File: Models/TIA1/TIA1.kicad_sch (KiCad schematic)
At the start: 0 parts

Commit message: Save progress
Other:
- note added: "Input: 15V power Input: -15V power Input: current Output: voltage Ground connection(s) not yet elaborated"
- note removed: "Input: 15V power (grounded interconnect) Input: -15V power (grounded interconnect) Input: current Output: voltage (grounded interconnect)"
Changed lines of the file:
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@@
 	(generator_version "9.0")
 	(paper "A4")
-	(text "Input: 15V power (grounded interconnect)\nInput: -15V power (grounded interconnect)\nInput: current\nOutput: voltage (grounded interconnect)"
+	(text "Input: 15V power\nInput: -15V power\nInput: current\nOutput: voltage\n\nGround connection(s) not yet elaborated"
 		(exclude_from_sim no)
 		(at 158.242 76.962 0)
@@
 		)
 		(instances
-			(project "TransimpedanceAmplifier"
+			(project "TIA1"
 				(path "/f19129fc-f916-4692-924c-ee308c6b3e1d"
 					(page "2")

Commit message: Save progress
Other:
- note added: "Input: 15V power Input: -15V power Input: current Output: voltage"
- note removed: "Input: 15V power Input: -15V power Input: current Output: voltage Ground connection(s) not yet elaborated"
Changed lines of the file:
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@@
 	(generator_version "9.0")
 	(paper "A4")
-	(text "Input: 15V power\nInput: -15V power\nInput: current\nOutput: voltage\n\nGround connection(s) not yet elaborated"
+	(text "Input: 15V power\nInput: -15V power\nInput: current\nOutput: voltage"
 		(exclude_from_sim no)
 		(at 158.242 76.962 0)
@@
 	(sheet
 		(at 101.6 76.2)
-		(size 50.8 50.8)
+		(size 50.8 25.4)
 		(exclude_from_sim no)
 		(in_bom yes)
@@
 		)
 		(property "Sheetfile" "Amplifier.kicad_sch"
-			(at 101.6 127.5846 0)
+			(at 101.6 102.1846 0)
 			(effects
 				(font

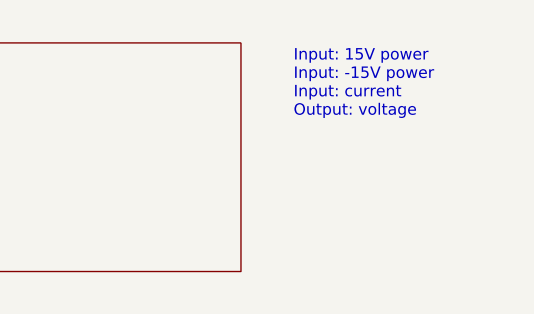
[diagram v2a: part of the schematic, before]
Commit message: Finished with the chips for the transimpedance amplifiers
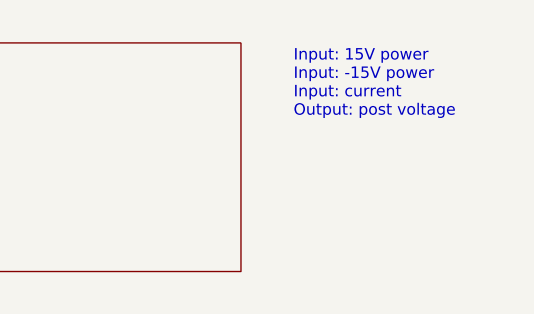
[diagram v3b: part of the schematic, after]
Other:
- note added: "Input: 15V power Input: -15V power Input: current Output: post voltage"
- note removed: "Input: 15V power Input: -15V power Input: current Output: voltage"
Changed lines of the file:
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@@
 	(generator_version "9.0")
 	(paper "A4")
-	(text "Input: 15V power\nInput: -15V power\nInput: current\nOutput: voltage"
+	(text "Input: 15V power\nInput: -15V power\nInput: current\nOutput: post voltage"
 		(exclude_from_sim no)
 		(at 158.242 76.962 0)

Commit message: Save progress
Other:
- sheet Amplifier ports: added -15V, 15V, Current, PostVoltage; removed none
- note removed: "Input: 15V power Input: -15V power Input: current Output: post voltage"
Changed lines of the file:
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@@
 	(generator_version "9.0")
 	(paper "A4")
-	(text "Input: 15V power\nInput: -15V power\nInput: current\nOutput: post voltage"
-		(exclude_from_sim no)
-		(at 158.242 76.962 0)
-		(effects
-			(font
-				(size 1.27 1.27)
-			)
-			(justify left top)
-		)
-	)
 	(sheet
 		(at 101.6 76.2)
@@
 			)
 		)
+		(pin "-15V" input
+			(at 147.32 101.6 270)
+			(effects
+				(font
+					(size 1.27 1.27)
+				)
+				(justify left)
+			)
+		)
+		(pin "15V" input
+			(at 147.32 76.2 90)
+			(effects
+				(font
+					(size 1.27 1.27)
+				)
+				(justify right)
+			)
+		)
+		(pin "Current" input
+			(at 101.6 88.9 180)
+			(effects
+				(font
+					(size 1.27 1.27)
+				)
+				(justify left)
+			)
+		)
+		(pin "PostVoltage" output
+			(at 152.4 88.9 0)
+			(effects
+				(font
+					(size 1.27 1.27)
+				)
+				(justify right)
+			)
+		)

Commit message: Save progress
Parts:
- added C3, C4: 100 nF, 0603, symbol Device:C
- added J1: Conn_01x08_Socket, symbol Connector:Conn_01x08_Socket
- added J3: Conn_01x03_Pin, symbol Connector:Conn_01x03_Pin
- added R1: 10, symbol Device:R_US
- added R3: 100M, 5%, 0603, symbol Device:R_US
- added U2: OPA828, symbol Amplifier_Operational:OP179GS
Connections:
- new net: J3.1 (Pin_1), R1.1
- new net -15V: C4.1, U2.4 (V-)
- new net 15V: C3.1, U2.7 (V+)
- new net BiasVoltage: J1.5 (Pin_5), J1.6 (Pin_6), J1.7 (Pin_7), J1.8 (Pin_8)
- new net Current: J1.1 (Pin_1), J1.2 (Pin_2), J1.3 (Pin_3), J1.4 (Pin_4), R3.1, U2.2 (-)
- new net GND: C3.2, C4.2, J3.3 (Pin_3), R1.2
- new net ISO_GND: J3.2 (Pin_2), U2.3 (+)
- new net PostVoltage: R3.2, U2.6
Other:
- removed sheet Amplifier

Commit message: Save progress
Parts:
- J3: now left out of the parts list
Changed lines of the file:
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@@
 		(unit 1)
 		(exclude_from_sim no)
-		(in_bom yes)
+		(in_bom no)
 		(on_board yes)
 		(dnp no)
@@
 			(at 215.9 106.68 0)
 			(effects
+				(font
+					(size 1.27 1.27)
+				)
+				(hide yes)
+			)
+		)
+		(property "Purchase Link" ""
+			(at 215.9 106.68 0)
+			(effects

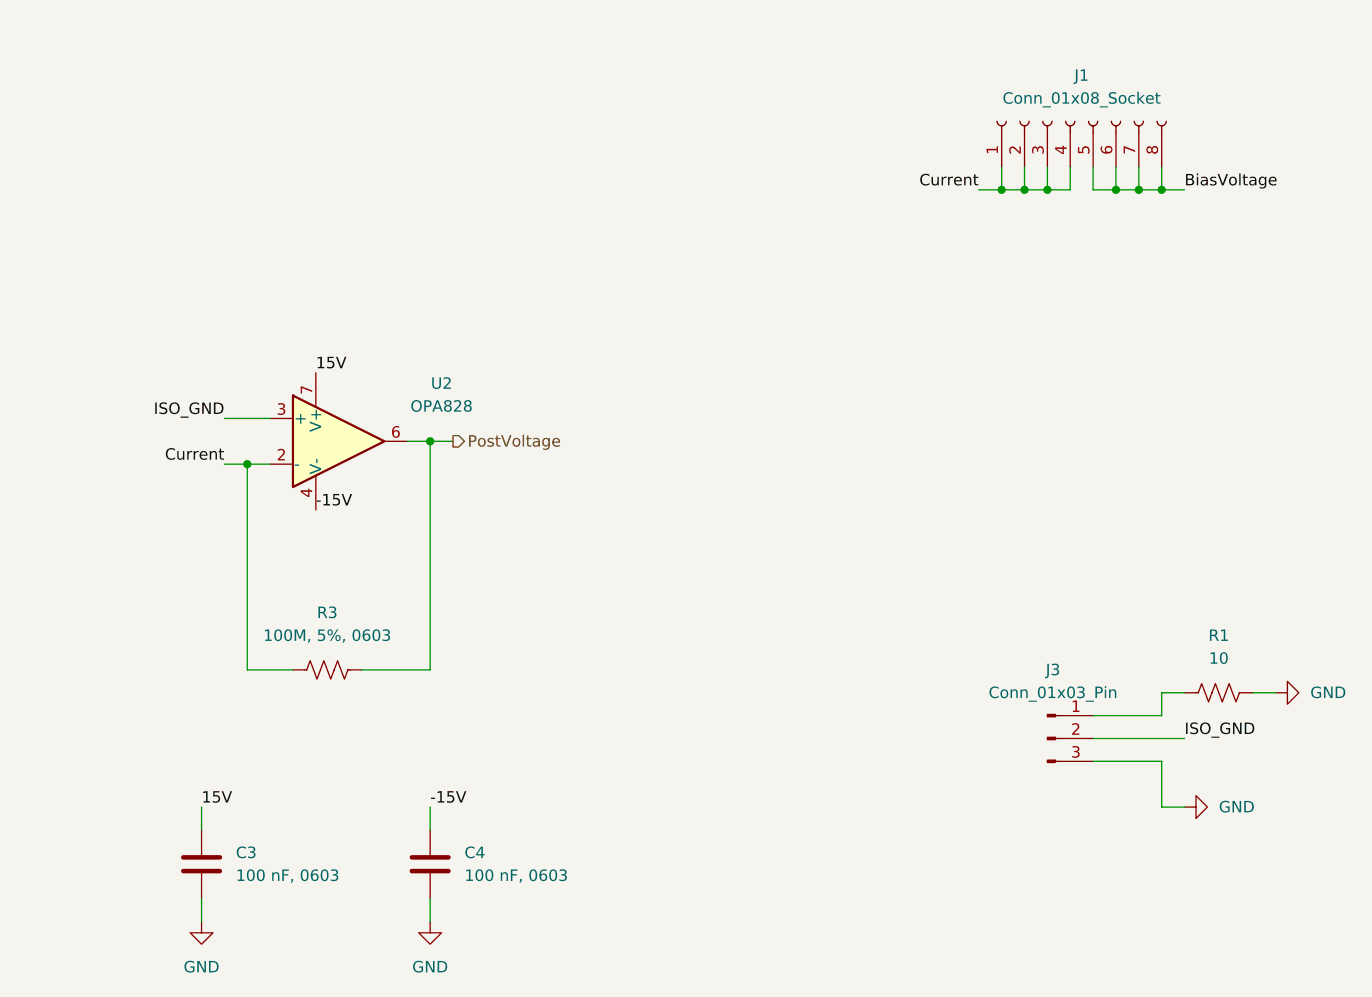
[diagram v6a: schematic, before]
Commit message: Connectors should be fully specified now
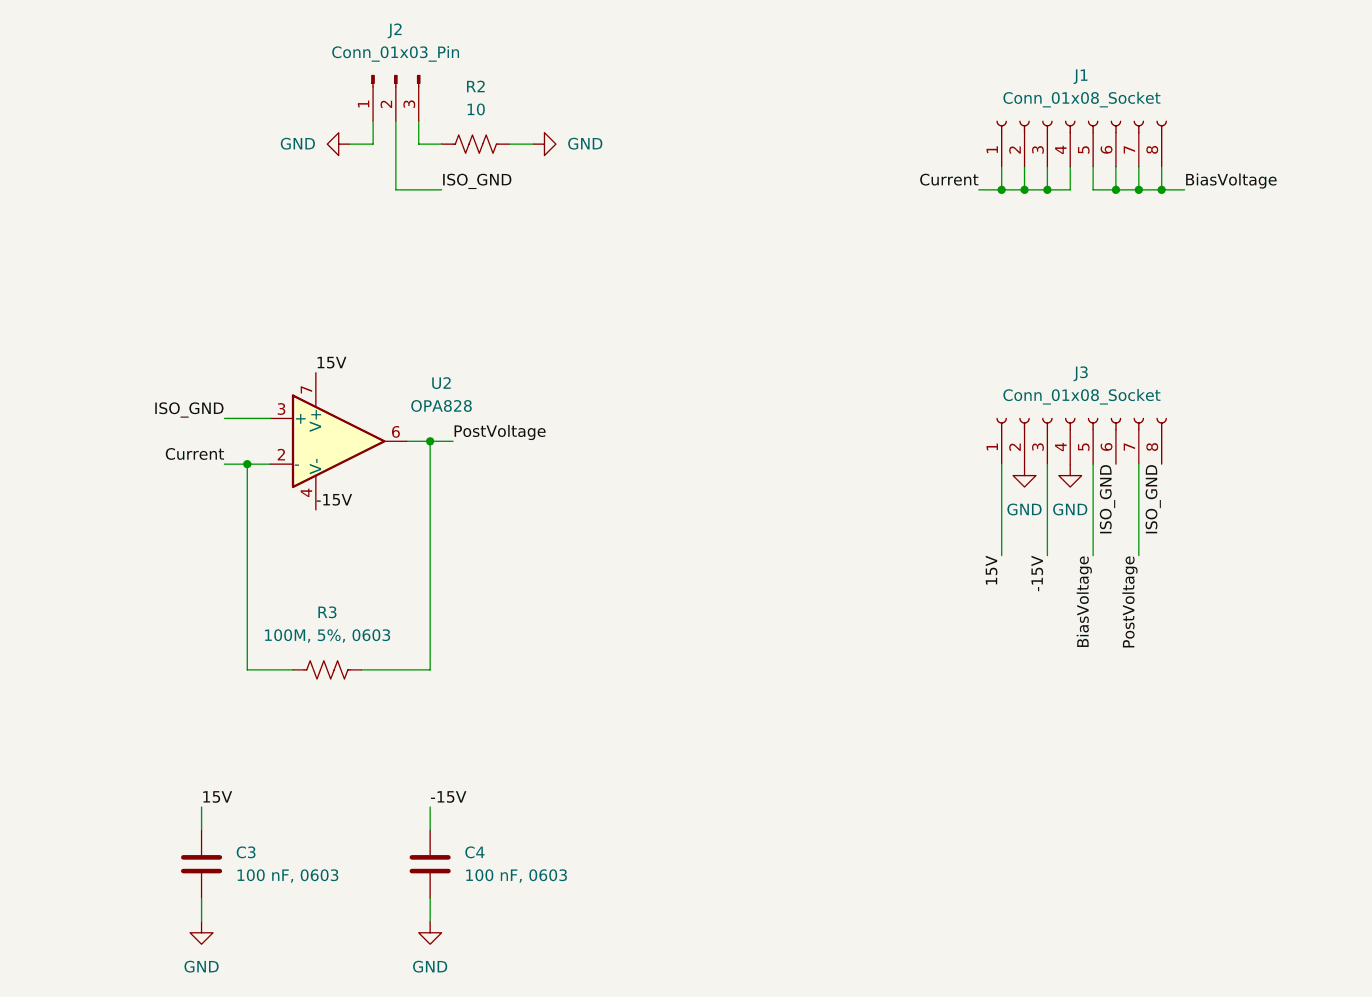
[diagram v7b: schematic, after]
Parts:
- removed J3: Conn_01x03_Pin, symbol Connector:Conn_01x03_Pin
- removed R1: 10, symbol Device:R_US
- added J2: Conn_01x03_Pin, symbol Connector:Conn_01x03_Pin
- added J3: Conn_01x08_Socket, symbol Connector:Conn_01x08_Socket
- added R2: 10, symbol Device:R_US
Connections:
- net -15V: now also J3.3 (Pin_3)
- net 15V: now also J3.1 (Pin_1)
- net BiasVoltage: now also J3.5 (Pin_5)
- net GND: now also J2.1 (Pin_1), J3.2 (Pin_2), J3.4 (Pin_4), R2.2
- net ISO_GND: now also J2.2 (Pin_2), J3.6 (Pin_6), J3.8 (Pin_8)
- net PostVoltage: now also J3.7 (Pin_7)
- new net: J2.3 (Pin_3), R2.1

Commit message: Passes ERC
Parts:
- renumbered C3 to C1, C4 to C2, J2 to J1, J1 to J2, R3 to R1, U2 to U1
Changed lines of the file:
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@@
 		(dnp no)
 		(fields_autoplaced yes)
-		(property "Reference" "J1"
+		(property "Reference" "J2"
 			(at 219.71 33.02 90)
 			(effects
@@
 			(project ""
 				(path "/f19129fc-f916-4692-924c-ee308c6b3e1d"
-					(reference "J1")
+					(reference "J2")
 					(unit 1)
 				)
@@
 		(dnp no)
 		(fields_autoplaced yes)
-		(property "Reference" "U2"
+		(property "Reference" "U1"
 			(at 148.59 67.2398 0)
 			(effects
@@
 			(project "TIA1"
 				(path "/f19129fc-f916-4692-924c-ee308c6b3e1d"
-					(reference "U2")
+					(reference "U1")
 					(unit 1)
 				)
@@
 		(dnp no)
 		(fields_autoplaced yes)
-		(property "Reference" "R3"
+		(property "Reference" "R1"
 			(at 135.89 92.71 90)
 			(effects
@@
 			(project "TIA1"
 				(path "/f19129fc-f916-4692-924c-ee308c6b3e1d"
-					(reference "R3")
+					(reference "R1")
 					(unit 1)
 				)
@@
 		(on_board yes)
 		(dnp no)
-		(property "Reference" "J2"
+		(property "Reference" "J1"
 			(at 143.51 27.94 90)
 			(effects
@@
 			(project "TIA1"
 				(path "/f19129fc-f916-4692-924c-ee308c6b3e1d"
-					(reference "J2")
+					(reference "J1")
 					(unit 1)
 				)
@@
 		(dnp no)
 		(fields_autoplaced yes)
-		(property "Reference" "#PWR05"
+		(property "Reference" "#PWR03"
 			(at 147.32 133.35 0)
 			(effects
@@
 			(project "TIA1"
 				(path "/f19129fc-f916-4692-924c-ee308c6b3e1d"
-					(reference "#PWR05")
+					(reference "#PWR03")
 					(unit 1)
 				)
@@
 		(dnp no)
 		(fields_autoplaced yes)
-		(property "Reference" "#PWR01"
+		(property "Reference" "#PWR02"
 			(at 132.08 40.64 0)
 			(effects
@@
 			(project "TIA1"
 				(path "/f19129fc-f916-4692-924c-ee308c6b3e1d"
-					(reference "#PWR01")
+					(reference "#PWR02")
 					(unit 1)
 				)
@@
 		(dnp no)
 		(fields_autoplaced yes)
-		(property "Reference" "C3"
+		(property "Reference" "C1"
 			(at 125.73 119.3799 0)
 			(effects
@@
 			(project "TIA1"
 				(path "/f19129fc-f916-4692-924c-ee308c6b3e1d"
-					(reference "C3")
+					(reference "C1")
 					(unit 1)
 				)
@@
 		(dnp no)
 		(fields_autoplaced yes)
-		(property "Reference" "#PWR02"
+		(property "Reference" "#PWR04"
 			(at 165.1 40.64 0)
 			(effects
@@
 			(project "TIA1"
 				(path "/f19129fc-f916-4692-924c-ee308c6b3e1d"
-					(reference "#PWR02")
+					(reference "#PWR04")
 					(unit 1)
 				)
@@
 		(dnp no)
 		(fields_autoplaced yes)
-		(property "Reference" "#PWR04"
+		(property "Reference" "#PWR01"
 			(at 121.92 133.35 0)
 			(effects
@@
 			(project "TIA1"
 				(path "/f19129fc-f916-4692-924c-ee308c6b3e1d"
-					(reference "#PWR04")
+					(reference "#PWR01")
 					(unit 1)
 				)
@@
 		(dnp no)
 		(fields_autoplaced yes)
-		(property "Reference" "#PWR03"
+		(property "Reference" "#PWR05"
 			(at 213.36 82.55 0)
 			(effects
@@
 			(project ""
 				(path "/f19129fc-f916-4692-924c-ee308c6b3e1d"
-					(reference "#PWR03")
+					(reference "#PWR05")
 					(unit 1)
 				)
@@
 		(dnp no)
 		(fields_autoplaced yes)
-		(property "Reference" "C4"
+		(property "Reference" "C2"
 			(at 151.13 119.3799 0)
 			(effects
@@
 			(project "TIA1"
 				(path "/f19129fc-f916-4692-924c-ee308c6b3e1d"
-					(reference "C4")
-					(unit 1)
-				)
+					(reference "C2")
+					(unit 1)
+				)
